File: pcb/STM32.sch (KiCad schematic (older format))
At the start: 34 parts, among them J1 Conn_02x07_Odd_Even, Q5 2SC3325-Y, X1 ABM8G

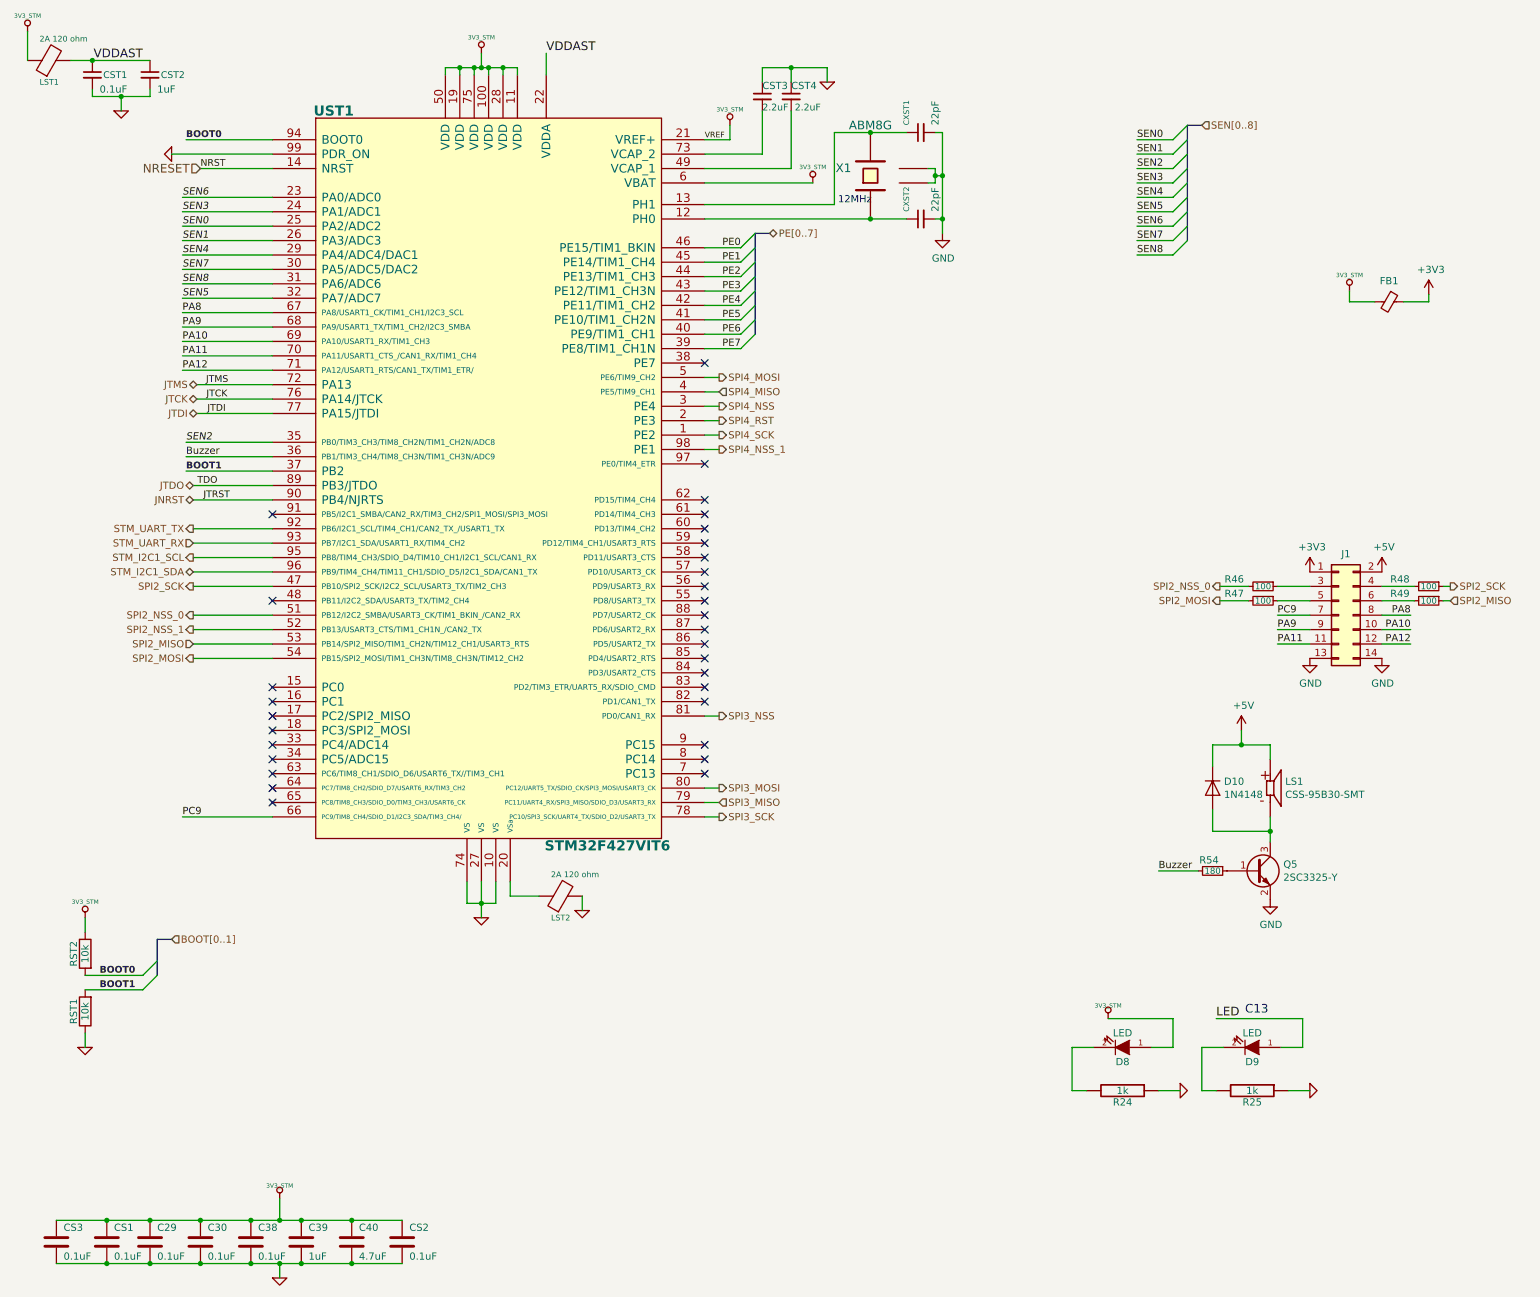
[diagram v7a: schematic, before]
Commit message: Solved connection problem with XCL214B333DR and it was added 3 leds to the board
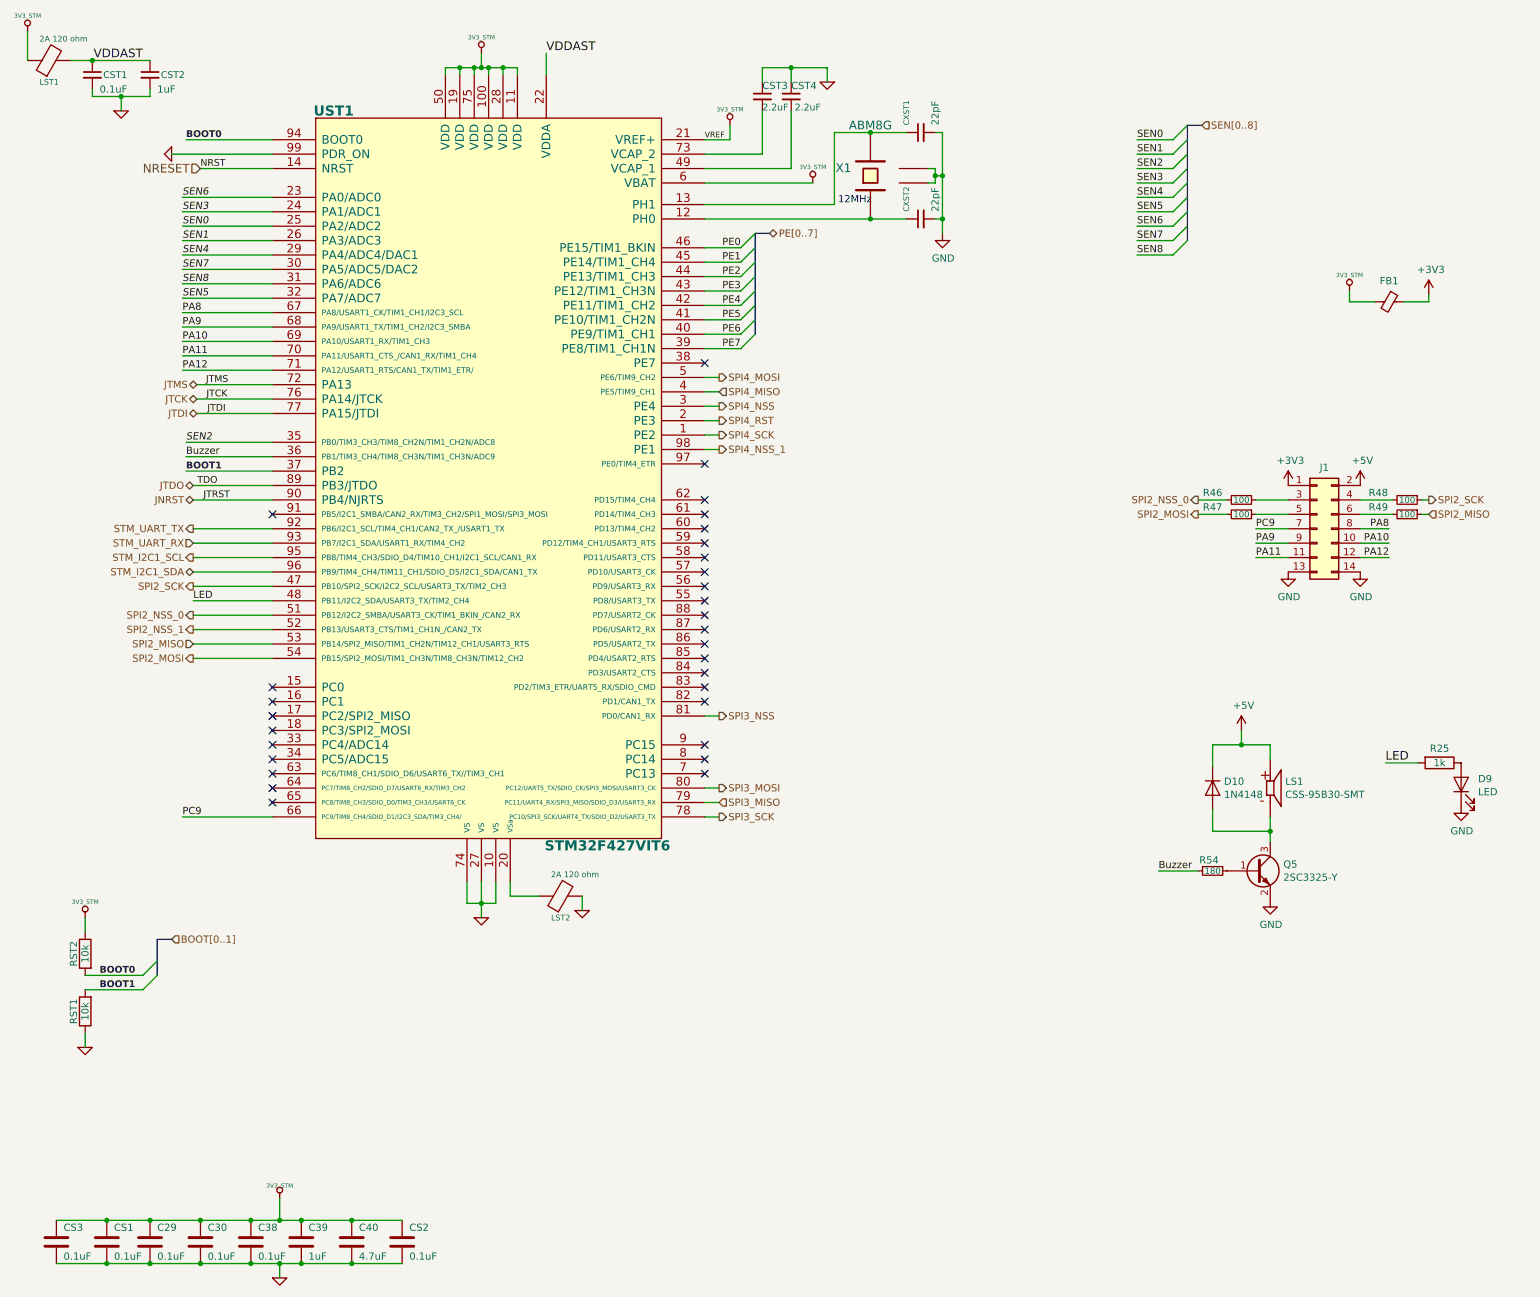
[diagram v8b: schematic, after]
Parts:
- removed D8, D9: LED, SM0603, symbol media_board:LED-RESCUE-stamp_mini_4_layers
- removed R24, R25: 1k, SM0603, symbol media_board:R-RESCUE-stamp_mini_4_layers
- added D9: LED, LED_SMD:LED_0603_1608Metric, symbol Device:LED
- added R25: 1k, Resistor_SMD:R_0402_1005Metric, symbol Device:R
- C39: footprint SM0603 -> Capacitor_SMD:C_0603_1608Metric
- C40: footprint SM1206 -> Capacitor_SMD:C_1206_3216Metric
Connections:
- net GND: now also D9.1 (K)
- net LED: now also UST1.48 (PB11/I2C2_SDA/USART3_TX/TIM2_CH4), R25.2
- new net: D9.2 (A), R25.1
- no-connect marks 31 -> 30
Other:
- note removed: "C13"
- moved on the sheet: J1, R46, R47, R48, R49
